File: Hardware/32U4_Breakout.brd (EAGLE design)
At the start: 39.4 x 25.4 mm, 33 parts, among them J1 AVR_SPI_PRG, U1 ATMEGA32U4, U2 3.3V_REG_LDOSMD, X1 USBSMD, Y1 16MHz

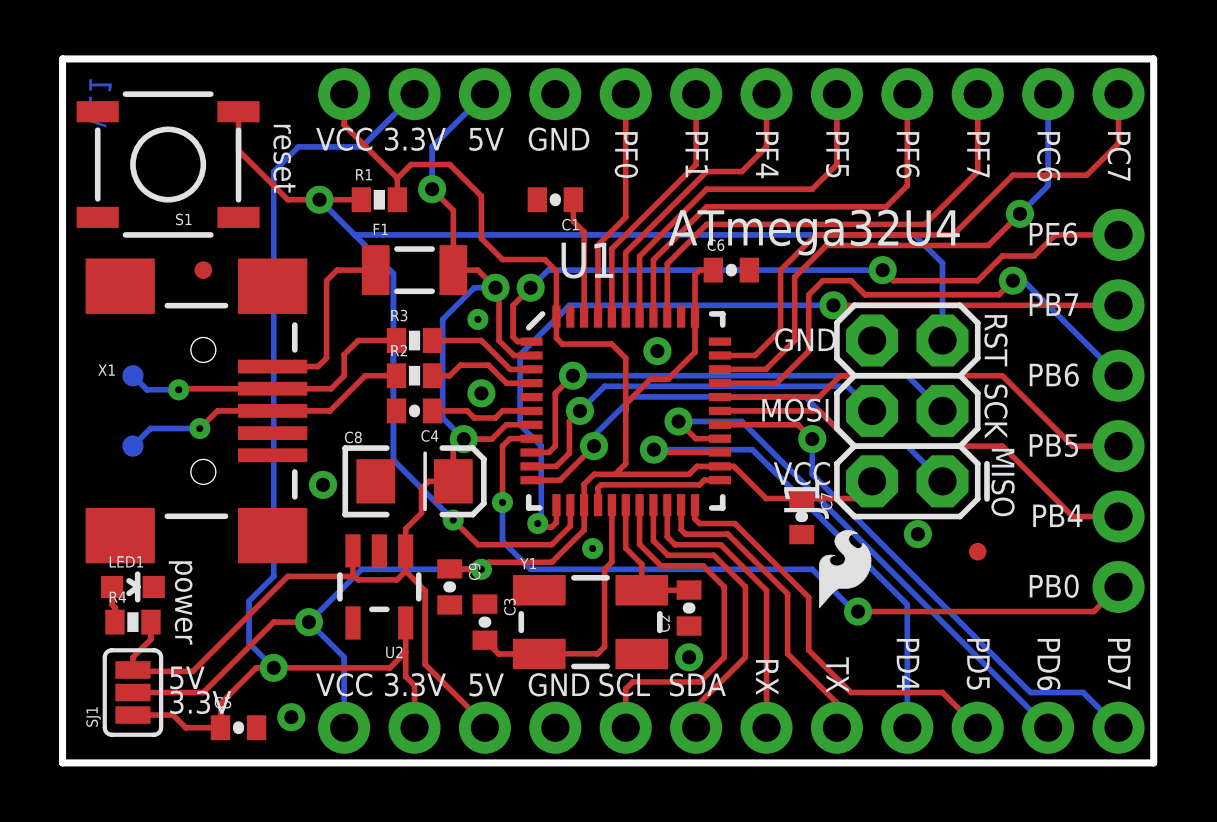
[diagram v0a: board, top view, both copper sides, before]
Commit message: Updated to v12 eagle files
Eagle files for QC board revision and schematic updates.
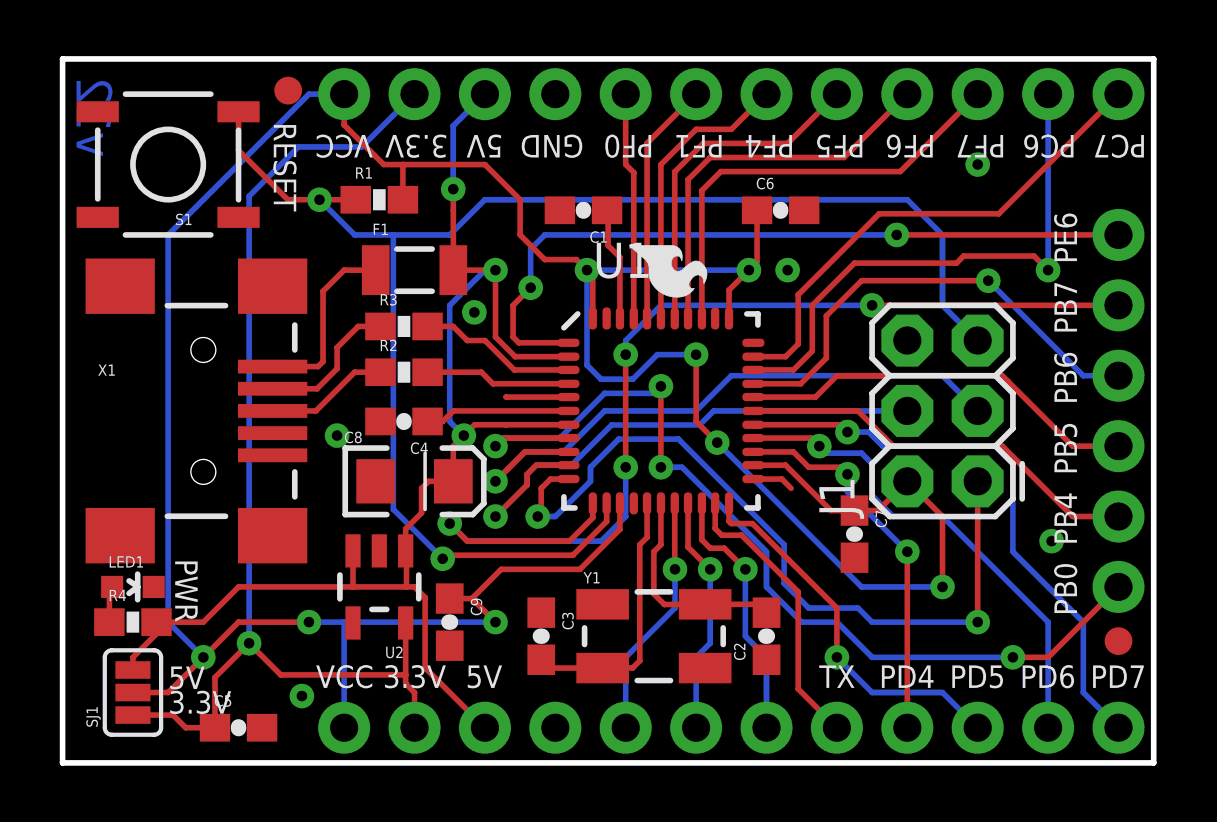
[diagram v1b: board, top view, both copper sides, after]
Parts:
- removed JP4: LOGO-SFENEW, SparkFun:SFE-NEW-WEBLOGO
- removed TP1, TP2: (no value), SparkFun:PAD.03X.03
- removed U$7: CREATIVE_COMMONS, SparkFun:CREATIVE_COMMONS
- added JP8: LOGO-SFENEW, SparkFun-Aesthetics:SFE-NEW-WEBLOGO
- C1, C2, C3, C4, C5, C6, C7, C9: device SparkFun:0402-CAP -> SparkFun-Capacitors:0603-CAP
- JP6, JP7: value FIDUCIALUFIDUCIAL -> FIDUCIAL1X2; device SparkFun:MICRO-FIDUCIAL -> SparkFun:FIDUCIAL-1X2
- R1, R2, R3, R4: device SparkFun:0402-RES -> SparkFun-Resistors:0603-RES
- U1: device SparkFun:QFN-44-NOPAD -> Testing:QFN-44-NOPAD_1:1
- moved JP5 14.8 mm to (20.4, 18.7), turned to 270 degrees
- moved U$6 13.7 mm to (16.0, 12.7)
- moved JP6 7.16 mm to (8.14, 24.3)
- moved JP7 6.02 mm to (38.1, 4.39)
- moved C2 2.97 mm to (25.4, 4.57)
- moved C6 2.80 mm to (25.9, 19.9)
- moved Y1 2.34 mm to (21.3, 4.57)
- moved C3 2.09 mm to (17.3, 4.57)
- moved C7 2.01 mm to (28.6, 8.26)
- moved J1 1.27 mm to (33.0, 10.2)
- moved C9 1.27 mm to (14.0, 5.08)
- moved U1 1.27 mm to (21.6, 12.7)
- moved C1 1.09 mm to (18.8, 19.9)
- moved R3 0.63 mm to (12.3, 15.7)
- moved C4 0.54 mm to (12.3, 12.3)
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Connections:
- net D+: no longer TP1.P$1
- net D-: no longer TP2.P$1
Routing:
- net VCC: track 66.9 -> 110.3 mm, vias 2 -> 8
- net MISO: track 17.6 -> 28.2 mm, vias 1 -> 2
- net PB7: track 30.2 -> 37.9 mm, vias 2 -> 4
- net D+: track 10.6 -> 4.47 mm, vias 1 -> 0
- net MOSI: track 14.5 -> 20.3 mm
- net D-: track 10.9 -> 5.27 mm, vias 1 -> 0
- net PB0: track 28.2 -> 33.7 mm, vias 2 -> 4
- net SCK: track 17.6 -> 22.6 mm
- net PD4: track 18.6 -> 13.8 mm, vias 1 -> 2
- net SCL: track 13.1 -> 8.83 mm, vias 0 -> 1
- net RST: track 50.2 -> 54.3 mm
- net SDA: track 11.1 -> 8.63 mm, vias 0 -> 1
- net PC7: track 20.6 -> 18.1 mm
- net N$2: track 5.35 -> 7.72 mm
- net PB6: track 18.9 -> 17.0 mm
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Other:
- board text added: "Breakout"
- board text added: "PWR"
- board text added: "RESET"
- board text added: "v12"
- board text removed: "power"
- board text removed: "reset"
- board text removed: "v11"

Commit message: Moved C5 and a couple tarces
Moved C5 and a couple traces to prevent problems with top silk on the
vcc jumper.
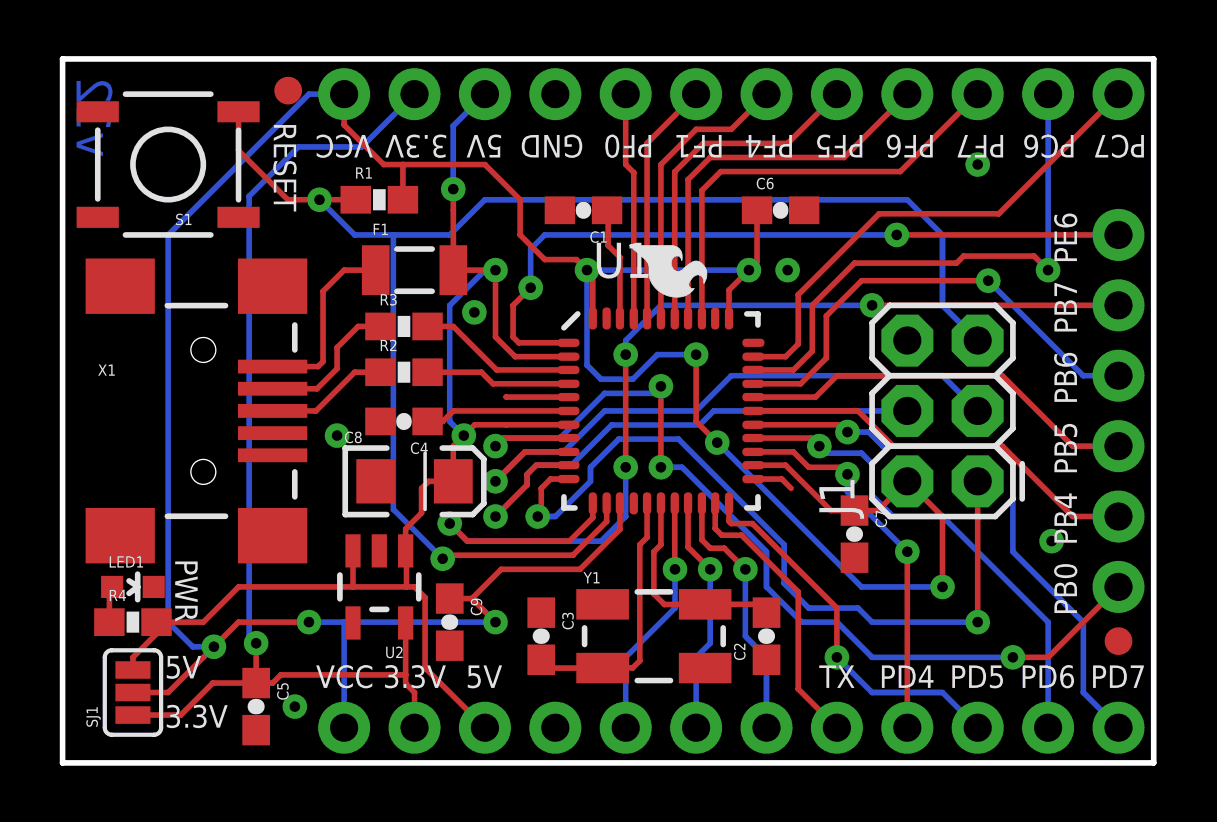
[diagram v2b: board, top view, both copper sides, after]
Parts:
- moved C5 0.99 mm to (6.99, 2.03), turned to 270 degrees
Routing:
- net 3.3V: track 40.4 -> 39.5 mm
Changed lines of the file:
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@@
 <text x="36.576" y="22.6568" size="0.8128" layer="21" font="vector" ratio="15" rot="SR180">PC6</text>
 <text x="39.116" y="22.6568" size="0.8128" layer="21" font="vector" ratio="15" rot="SR180">PC7</text>
-<text x="3.81" y="2.667" size="0.8128" layer="21" font="vector" ratio="15">5V</text>
-<text x="3.81" y="1.778" size="0.8128" layer="21" font="vector" ratio="15">3.3V</text>
+<text x="3.683" y="3.048" size="0.8128" layer="21" font="vector" ratio="15">5V</text>
+<text x="3.683" y="1.27" size="0.8128" layer="21" font="vector" ratio="15">3.3V</text>
 <text x="7.62" y="23.114" size="0.8128" layer="21" font="vector" ratio="15" rot="SR270">RESET</text>
 <text x="4.064" y="7.366" size="0.8128" layer="21" font="vector" ratio="15" rot="SR270">PWR</text>
@@
 <element name="C4" library="SparkFun-Capacitors" package="0603-CAP" value="1uF" x="12.319" y="12.319" rot="R180"/>
 <element name="U2" library="SparkFun" package="SOT23-5" value="3.3V_REG_LDOSMD" x="11.43" y="6.35" rot="R180"/>
-<element name="C5" library="SparkFun-Capacitors" package="0603-CAP" value="1uF" x="6.35" y="1.27"/>
+<element name="C5" library="SparkFun-Capacitors" package="0603-CAP" value="1uF" x="6.985" y="2.032" rot="R270"/>
 <element name="SJ1" library="SparkFun" package="SJ_3_PASTE2&amp;3" value="Power Select" x="2.54" y="2.54" rot="R90"/>
 <element name="C6" library="SparkFun-Capacitors" package="0603-CAP" value="0.1uF" x="25.908" y="19.939"/>
@@
 <contactref element="C9" pad="2"/>
 <via x="9.906" y="11.811" extent="1-16" drill="0.381"/>
-<via x="8.636" y="2.413" extent="1-16" drill="0.381"/>
+<via x="8.382" y="2.032" extent="1-16" drill="0.381"/>
 <via x="14.859" y="16.256" extent="1-16" drill="0.381"/>
 <polygon width="0.2032" layer="1" isolate="0.2032">
@@
 <wire x1="18.923" y1="14.351" x2="18.923" y2="17.78" width="0.2032" layer="16"/>
 <wire x1="8.89" y1="5.08" x2="6.35" y2="5.08" width="0.2032" layer="1"/>
-<wire x1="6.35" y1="5.08" x2="5.08" y2="3.81" width="0.2032" layer="1"/>
-<wire x1="5.08" y1="3.81" x2="3.81" y2="2.54" width="0.2032" layer="1"/>
 <wire x1="3.81" y1="2.54" x2="2.54" y2="2.54" width="0.2032" layer="1"/>
 <wire x1="10.16" y1="24.13" x2="8.89" y2="24.13" width="0.2032" layer="16"/>
 <wire x1="8.89" y1="24.13" x2="3.81" y2="19.05" width="0.2032" layer="16"/>
 <wire x1="10.16" y1="23.017" x2="10.16" y2="24.13" width="0.2032" layer="1"/>
-<via x="5.08" y="3.81" extent="1-16" drill="0.381"/>
+<via x="5.461" y="4.191" extent="1-16" drill="0.381"/>
 <wire x1="3.81" y1="19.05" x2="3.81" y2="5.08" width="0.2032" layer="16"/>
-<wire x1="3.81" y1="5.08" x2="5.08" y2="3.81" width="0.2032" layer="16"/>
+<wire x1="3.81" y1="5.08" x2="4.699" y2="4.191" width="0.2032" layer="16"/>
+<wire x1="4.699" y1="4.191" x2="5.461" y2="4.191" width="0.2032" layer="16"/>
+<wire x1="6.35" y1="5.08" x2="5.461" y2="4.191" width="0.2032" layer="1"/>
+<wire x1="3.81" y1="2.54" x2="5.461" y2="4.191" width="0.2032" layer="1"/>
 </signal>
 <signal name="AREF">
@@
 <contactref element="R3" pad="2"/>
 <contactref element="U1" pad="3"/>
-<wire x1="18.2535" y1="14.17886875" x2="16.30113125" y2="14.17886875" width="0.2032" layer="1"/>
-<wire x1="16.30113125" y1="14.17886875" x2="15.24" y2="15.24" width="0.2032" layer="1"/>
+<wire x1="18.2535" y1="14.17886875" x2="15.66613125" y2="14.17886875" width="0.2032" layer="1"/>
 <wire x1="13.169" y1="15.748" x2="14.097" y2="15.748" width="0.2032" layer="1"/>
-<wire x1="15.24" y1="15.24" x2="14.605" y2="15.24" width="0.2032" layer="1"/>
-<wire x1="14.605" y1="15.24" x2="14.097" y2="15.748" width="0.2032" layer="1"/>
+<wire x1="15.66613125" y1="14.17886875" x2="14.097" y2="15.748" width="0.2032" layer="1"/>
 </signal>
 <signal name="5V">
@@
 <contactref element="JP1" pad="2"/>
 <contactref element="JP2" pad="2"/>
-<wire x1="2.54" y1="1.7272" x2="3.9878" y2="1.7272" width="0.2032" layer="1"/>
-<wire x1="3.9878" y1="1.7272" x2="4.445" y2="1.27" width="0.2032" layer="1"/>
-<wire x1="4.445" y1="1.27" x2="5.5" y2="1.27" width="0.2032" layer="1"/>
+<wire x1="2.54" y1="1.7272" x2="4.2672" y2="1.7272" width="0.2032" layer="1"/>
 <wire x1="8.509" y1="22.225" x2="10.795" y2="22.225" width="0.2032" layer="16"/>
 <wire x1="10.795" y1="22.225" x2="12.7" y2="24.13" width="0.2032" layer="16"/>
-<via x="6.731" y="4.318" extent="1-16" drill="0.381"/>
-<wire x1="6.731" y1="4.318" x2="6.731" y2="20.447" width="0.2032" layer="16"/>
+<via x="6.985" y="4.318" extent="1-16" drill="0.381"/>
 <wire x1="6.731" y1="20.447" x2="8.509" y2="22.225" width="0.2032" layer="16"/>
 <wire x1="12.7" y1="1.27" x2="12.7" y2="2.54" width="0.2032" layer="1"/>
@@
 <wire x1="12.38" y1="2.86" x2="12.7" y2="2.54" width="0.2032" layer="1"/>
 <wire x1="12.38" y1="3.175" x2="7.874" y2="3.175" width="0.2032" layer="1"/>
-<wire x1="7.874" y1="3.175" x2="6.731" y2="4.318" width="0.2032" layer="1"/>
-<wire x1="5.5" y1="1.27" x2="5.5" y2="3.087" width="0.2032" layer="1"/>
-<wire x1="5.5" y1="3.087" x2="6.731" y2="4.318" width="0.2032" layer="1"/>
+<wire x1="4.2672" y1="1.7272" x2="5.422" y2="2.882" width="0.2032" layer="1"/>
+<wire x1="6.985" y1="2.882" x2="5.422" y2="2.882" width="0.2032" layer="1"/>
+<wire x1="6.985" y1="2.882" x2="6.985" y2="4.318" width="0.2032" layer="1"/>
+<wire x1="6.985" y1="2.882" x2="7.581" y2="2.882" width="0.2032" layer="1"/>
+<wire x1="7.581" y1="2.882" x2="7.874" y2="3.175" width="0.2032" layer="1"/>
+<wire x1="6.731" y1="20.447" x2="6.731" y2="4.572" width="0.2032" layer="16"/>
+<wire x1="6.731" y1="4.572" x2="6.985" y2="4.318" width="0.2032" layer="16"/>
 </signal>
 <signal name="MISO">
@@
 </signal>
 </signals>
+<errors>
+</errors>
 </board>
 </drawing>
